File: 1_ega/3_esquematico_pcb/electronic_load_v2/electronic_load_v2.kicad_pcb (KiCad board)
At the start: 2 copper layers, 100 x 50 mm, 67 parts, among them J1 Encoder, J11 LOAD, J12 Memoria SD, J13 LCD, J15 VCC, J16 RTC, J17 EGB, J3 GND, J6 RPico PWR, J7 GND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

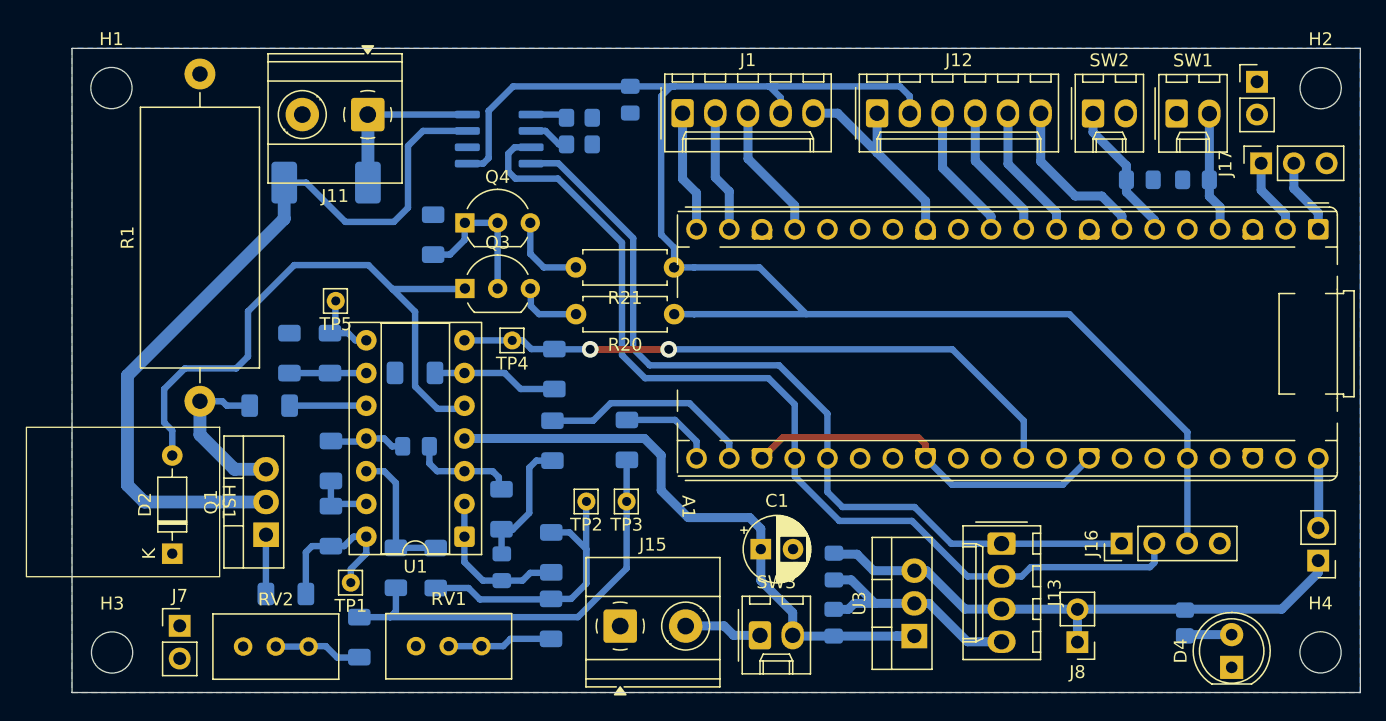
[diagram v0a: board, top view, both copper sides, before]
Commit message: fix: add text and logo
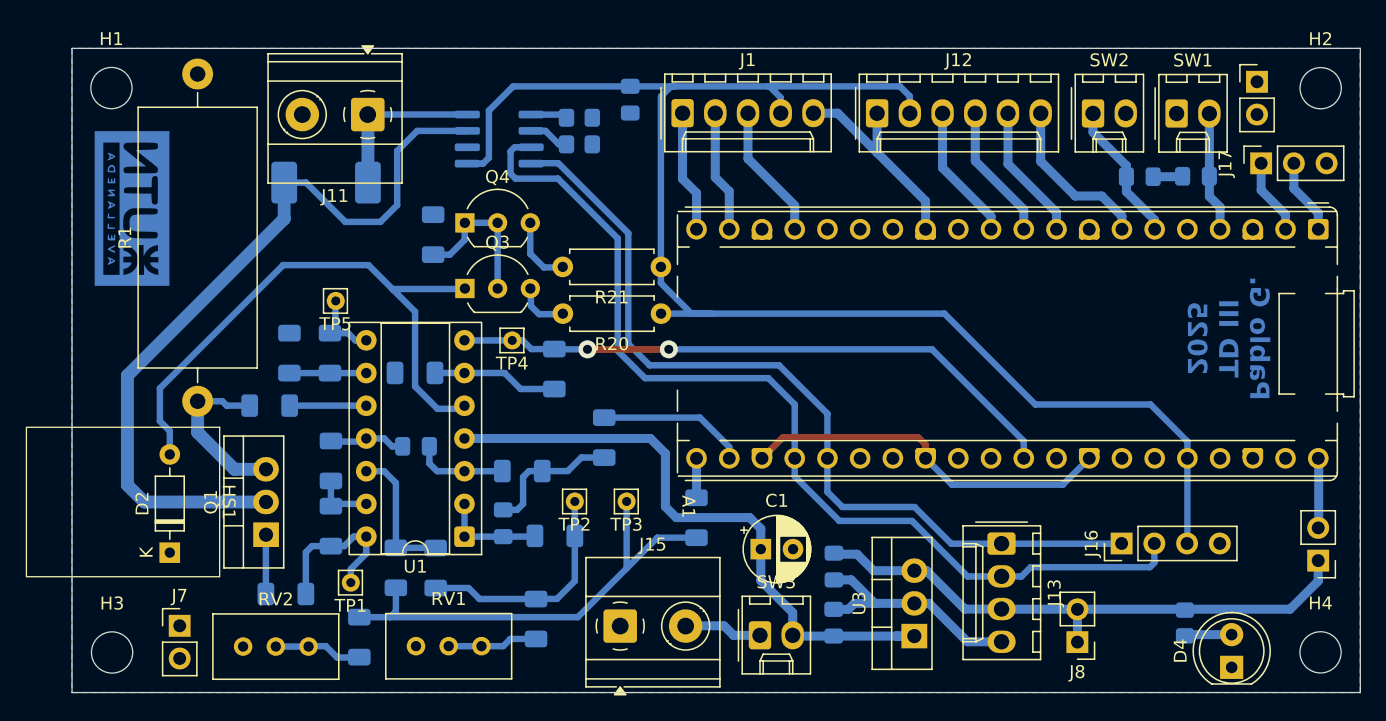
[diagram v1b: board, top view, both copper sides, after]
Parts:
- added G***: LOGO, LOGO, B.Cu at (24.7, 69.9)
- moved R16 8.10 mm to (68.5, 93.9)
- moved R7 4.03 mm to (61.3, 87.7)
- moved C5 3.42 mm to (53.5, 94.4)
- moved R6 3.37 mm to (55.0, 90.3), turned to 180 degrees
- moved R11 1.31 mm to (57.5, 95.3), turned to 0 degrees
- moved R12 1.16 mm to (56.0, 101.8)
- moved R20 1.02 mm to (65.7, 78.1)
- moved R21 1.02 mm to (65.7, 74.5)
- moved TP2 0.90 mm to (59.0, 92.7)
- moved C3 0.27 mm to (107.2, 67.4)
- moved C4 0.24 mm to (102.9, 67.5)
- moved D2 0.21 mm to (27.6, 96.6)
- moved R1 0.18 mm to (29.8, 84.9)
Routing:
- net MOS_SK: track 24.9 -> 17.9 mm
- net +3V3: track 122.5 -> 117.1 mm
- net MOS_PWM: track 16.8 -> 11.5 mm
- net MOS_EN: track 7.45 -> 3.10 mm
- net Net-(U1A--): track 12.1 -> 8.05 mm
- net MOS_OFFSET: track 33.3 -> 36.4 mm
- net GND: track 70.1 -> 72.5 mm
- net Net-(D2-A): track 48.5 -> 46.8 mm
- net Net-(R12-Pad1): track 8.18 -> 7.01 mm
- net Net-(Q4-E): track 6.38 -> 5.38 mm
- net Net-(Q3-E): track 5.14 -> 4.13 mm
- net Net-(U1A-+): track 8.18 -> 7.24 mm
- net TEMP_DIODE: track 49.3 -> 48.4 mm
- net VCC: track 48.1 -> 48.9 mm
- net Net-(C5-Pad1): track 10.2 -> 10.7 mm
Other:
- board text added: "Pablo G. TD III 2025"
